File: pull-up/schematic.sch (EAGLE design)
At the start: 2 parts

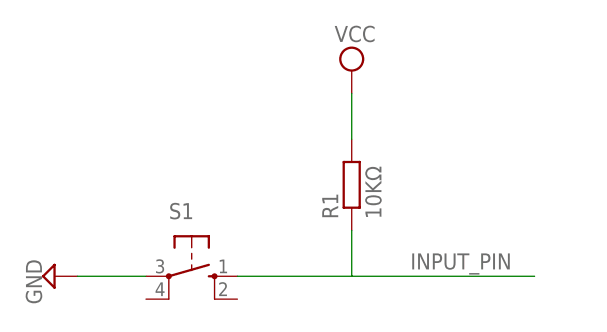
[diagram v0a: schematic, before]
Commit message: update schematics and remove .epf files
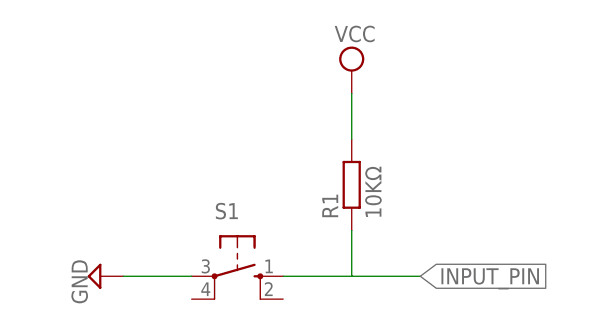
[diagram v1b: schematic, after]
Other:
- moved on the sheet: S1
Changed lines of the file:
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@@
 </plain>
 <instances>
-<instance part="SUPPLY1" gate="GND" x="-7.62" y="43.18" rot="R270"/>
+<instance part="SUPPLY1" gate="GND" x="-2.54" y="43.18" rot="R270"/>
 <instance part="SUPPLY3" gate="G$1" x="25.4" y="66.04"/>
-<instance part="S1" gate="1" x="7.62" y="43.18" rot="R270"/>
+<instance part="S1" gate="1" x="12.7" y="43.18" rot="R270"/>
 <instance part="R1" gate="G$1" x="25.4" y="53.34" rot="R90"/>
 </instances>
@@
 <pinref part="SUPPLY1" gate="GND" pin="GND"/>
 <pinref part="S1" gate="1" pin="P"/>
-<wire x1="-5.08" y1="43.18" x2="2.54" y2="43.18" width="0.1524" layer="91"/>
+<wire x1="0" y1="43.18" x2="7.62" y2="43.18" width="0.1524" layer="91"/>
 </segment>
 </net>
@@
 <segment>
 <pinref part="S1" gate="1" pin="S"/>
-<wire x1="12.7" y1="43.18" x2="25.4" y2="43.18" width="0.1524" layer="91"/>
+<wire x1="17.78" y1="43.18" x2="25.4" y2="43.18" width="0.1524" layer="91"/>
 <pinref part="R1" gate="G$1" pin="1"/>
-<wire x1="25.4" y1="43.18" x2="45.72" y2="43.18" width="0.1524" layer="91"/>
+<wire x1="25.4" y1="43.18" x2="33.02" y2="43.18" width="0.1524" layer="91"/>
 <wire x1="25.4" y1="48.26" x2="25.4" y2="43.18" width="0.1524" layer="91"/>
-<label x="43.18" y="45.72" size="1.778" layer="95" rot="R180"/>
+<label x="33.02" y="43.18" size="1.778" layer="95" rot="MR180" xref="yes"/>
 </segment>
 </net>
